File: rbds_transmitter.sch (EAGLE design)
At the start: 136 parts, among them J2 AVRISP-6, Q1 P-CH, Q2 P-Ch, Q3 P-Ch, T1 ATB3225-75034CT, T2 ATB3225-75034CT, U1 MAX2606, U2 TS974, U3 TS974, U4 MAX1551, U5 ATMEGA328, U6 TPS61030, U7 MCP4812, X1 16Mhz

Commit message: working
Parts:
- D1: device adafruit:DIODESMA -> adafruit:DIODESOD-123
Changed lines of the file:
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@@
 <grid distance="0.1" unitdist="inch" unit="inch" style="lines" multiple="1" display="no" altdistance="0.01" altunitdist="inch" altunit="inch"/>
 <layers>
-<layer number="1" name="Top" color="4" fill="1" visible="no" active="no"/>
-<layer number="2" name="Route2" color="1" fill="3" visible="no" active="no"/>
-<layer number="3" name="Route3" color="4" fill="3" visible="no" active="no"/>
-<layer number="4" name="Route4" color="1" fill="4" visible="no" active="no"/>
-<layer number="5" name="Route5" color="4" fill="4" visible="no" active="no"/>
-<layer number="6" name="Route6" color="1" fill="8" visible="no" active="no"/>
-<layer number="7" name="Route7" color="4" fill="8" visible="no" active="no"/>
-<layer number="8" name="Route8" color="1" fill="2" visible="no" active="no"/>
-<layer number="9" name="Route9" color="4" fill="2" visible="no" active="no"/>
-<layer number="10" name="Route10" color="1" fill="7" visible="no" active="no"/>
-<layer number="11" name="Route11" color="4" fill="7" visible="no" active="no"/>
-<layer number="12" name="Route12" color="1" fill="5" visible="no" active="no"/>
-<layer number="13" name="Route13" color="4" fill="5" visible="no" active="no"/>
-<layer number="14" name="Route14" color="1" fill="6" visible="no" active="no"/>
-<layer number="15" name="Route15" color="4" fill="6" visible="no" active="no"/>
-<layer number="16" name="Bottom" color="1" fill="1" visible="no" active="no"/>
-<layer number="17" name="Pads" color="2" fill="1" visible="no" active="no"/>
-<layer number="18" name="Vias" color="2" fill="1" visible="no" active="no"/>
-<layer number="19" name="Unrouted" color="6" fill="1" visible="no" active="no"/>
-<layer number="20" name="Dimension" color="15" fill="1" visible="no" active="no"/>
-<layer number="21" name="tPlace" color="7" fill="1" visible="no" active="no"/>
-<layer number="22" name="bPlace" color="7" fill="1" visible="no" active="no"/>
-<layer number="23" name="tOrigins" color="15" fill="1" visible="no" active="no"/>
-<layer number="24" name="bOrigins" color="15" fill="1" visible="no" active="no"/>
-<layer number="25" name="tNames" color="7" fill="1" visible="no" active="no"/>
-<layer number="26" name="bNames" color="7" fill="1" visible="no" active="no"/>
-<layer number="27" name="tValues" color="7" fill="1" visible="no" active="no"/>
-<layer number="28" name="bValues" color="7" fill="1" visible="no" active="no"/>
+<layer number="1" name="Top" color="4" fill="1" visible="yes" active="no"/>
+<layer number="2" name="Route2" color="1" fill="3" visible="yes" active="no"/>
+<layer number="3" name="Route3" color="4" fill="3" visible="yes" active="no"/>
+<layer number="4" name="Route4" color="1" fill="4" visible="yes" active="no"/>
+<layer number="5" name="Route5" color="4" fill="4" visible="yes" active="no"/>
+<layer number="6" name="Route6" color="1" fill="8" visible="yes" active="no"/>
+<layer number="7" name="Route7" color="4" fill="8" visible="yes" active="no"/>
+<layer number="8" name="Route8" color="1" fill="2" visible="yes" active="no"/>
+<layer number="9" name="Route9" color="4" fill="2" visible="yes" active="no"/>
+<layer number="10" name="Route10" color="1" fill="7" visible="yes" active="no"/>
+<layer number="11" name="Route11" color="4" fill="7" visible="yes" active="no"/>
+<layer number="12" name="Route12" color="1" fill="5" visible="yes" active="no"/>
+<layer number="13" name="Route13" color="4" fill="5" visible="yes" active="no"/>
+<layer number="14" name="Route14" color="1" fill="6" visible="yes" active="no"/>
+<layer number="15" name="Route15" color="4" fill="6" visible="yes" active="no"/>
+<layer number="16" name="Bottom" color="1" fill="1" visible="yes" active="no"/>
+<layer number="17" name="Pads" color="2" fill="1" visible="yes" active="no"/>
+<layer number="18" name="Vias" color="2" fill="1" visible="yes" active="no"/>
+<layer number="19" name="Unrouted" color="6" fill="1" visible="yes" active="no"/>
+<layer number="20" name="Dimension" color="15" fill="1" visible="yes" active="no"/>
+<layer number="21" name="tPlace" color="7" fill="1" visible="yes" active="no"/>
+<layer number="22" name="bPlace" color="7" fill="1" visible="yes" active="no"/>
+<layer number="23" name="tOrigins" color="15" fill="1" visible="yes" active="no"/>
+<layer number="24" name="bOrigins" color="15" fill="1" visible="yes" active="no"/>
+<layer number="25" name="tNames" color="7" fill="1" visible="yes" active="no"/>
+<layer number="26" name="bNames" color="7" fill="1" visible="yes" active="no"/>
+<layer number="27" name="tValues" color="7" fill="1" visible="yes" active="no"/>
+<layer number="28" name="bValues" color="7" fill="1" visible="yes" active="no"/>
 <layer number="29" name="tStop" color="7" fill="3" visible="no" active="no"/>
 <layer number="30" name="bStop" color="7" fill="6" visible="no" active="no"/>
@@
 <layer number="35" name="tGlue" color="7" fill="4" visible="no" active="no"/>
 <layer number="36" name="bGlue" color="7" fill="5" visible="no" active="no"/>
-<layer number="37" name="tTest" color="7" fill="1" visible="no" active="no"/>
-<layer number="38" name="bTest" color="7" fill="1" visible="no" active="no"/>
+<layer number="37" name="tTest" color="7" fill="1" visible="yes" active="no"/>
+<layer number="38" name="bTest" color="7" fill="1" visible="yes" active="no"/>
 <layer number="39" name="tKeepout" color="4" fill="11" visible="no" active="no"/>
 <layer number="40" name="bKeepout" color="1" fill="11" visible="no" active="no"/>
@@
 <layer number="44" name="Drills" color="7" fill="1" visible="no" active="no"/>
 <layer number="45" name="Holes" color="7" fill="1" visible="no" active="no"/>
-<layer number="46" name="Milling" color="3" fill="1" visible="no" active="no"/>
-<layer number="47" name="Measures" color="7" fill="1" visible="no" active="no"/>
-<layer number="48" name="Document" color="7" fill="1" visible="no" active="no"/>
-<layer number="49" name="Reference" color="7" fill="1" visible="no" active="no"/>
-<layer number="50" name="dxf" color="7" fill="1" visible="no" active="no"/>
-<layer number="51" name="tDocu" color="7" fill="1" visible="no" active="no"/>
-<layer number="52" name="bDocu" color="7" fill="1" visible="no" active="no"/>
-<layer number="53" name="tGND_GNDA" color="7" fill="9" visible="no" active="no"/>
-<layer number="54" name="bGND_GNDA" color="1" fill="9" visible="no" active="no"/>
-<layer number="56" name="wert" color="7" fill="1" visible="no" active="no"/>
-<layer number="57" name="tCAD" color="7" fill="1" visible="no" active="no"/>
+<layer number="46" name="Milling" color="3" fill="1" visible="yes" active="no"/>
+<layer number="47" name="Measures" color="7" fill="1" visible="yes" active="no"/>
+<layer number="48" name="Document" color="7" fill="1" visible="yes" active="no"/>
+<layer number="49" name="Reference" color="7" fill="1" visible="yes" active="no"/>
+<layer number="50" name="dxf" color="7" fill="1" visible="yes" active="no"/>
+<layer number="51" name="tDocu" color="7" fill="1" visible="yes" active="no"/>
+<layer number="52" name="bDocu" color="7" fill="1" visible="yes" active="no"/>
+<layer number="53" name="tGND_GNDA" color="7" fill="9" visible="yes" active="no"/>
+<layer number="54" name="bGND_GNDA" color="1" fill="9" visible="yes" active="no"/>
+<layer number="56" name="wert" color="7" fill="1" visible="yes" active="no"/>
+<layer number="57" name="tCAD" color="7" fill="1" visible="yes" active="no"/>
 <layer number="91" name="Nets" color="2" fill="1" visible="yes" active="yes"/>
 <layer number="92" name="Busses" color="1" fill="1" visible="yes" active="yes"/>
@@
 <part name="GND39" library="sparkfun" deviceset="GND" device=""/>
 <part name="Q1" library="sparkfun" deviceset="MOSFET-PCHANNEL" device="SMD" value="P-CH"/>
-<part name="D1" library="adafruit" deviceset="DIODE" device="SMA"/>
+<part name="D1" library="adafruit" deviceset="DIODE" device="SOD-123"/>
 <part name="R15" library="adafruit" deviceset="R-US_" device="R1206" value="100k"/>
 <part name="GND41" library="sparkfun" deviceset="GND" device=""/>

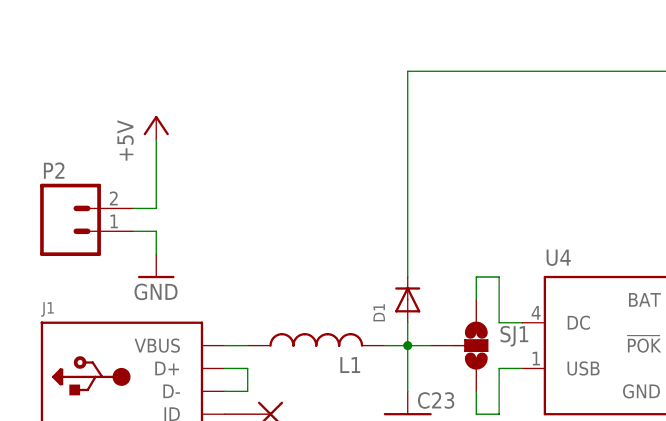
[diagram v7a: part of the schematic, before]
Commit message: schematic update: corrected 5v connection
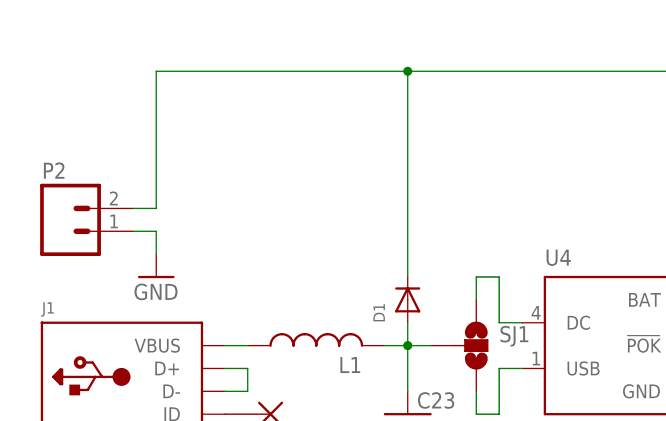
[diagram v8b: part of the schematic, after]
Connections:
- removed net N$6: D1.C, Q1.S, SW1.S
- new net N$15: D1.C, P2.2, Q1.S, SW1.S
- net +5V: no longer P2.2
